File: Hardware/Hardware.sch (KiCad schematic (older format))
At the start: 1 part

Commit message: Some hardware dev
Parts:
- added C? (x2): C, symbol Device:C
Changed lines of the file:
@@
+	1    0    0    -1
+$EndComp
+$Comp
+L Device:C C?
+U 1 1 62087589
+P 3450 1550
+F 0 "C?" H 3565 1596 50  0000 L CNN
+F 1 "C" H 3565 1505 50  0000 L CNN
+F 2 "" H 3488 1400 50  0001 C CNN
+F 3 "~" H 3450 1550 50  0001 C CNN
+	1    3450 1550
+	1    0    0    -1
+$EndComp
+$Comp
+L Device:C C?
+U 1 1 620890B1
+P 2950 1550
+F 0 "C?" H 3065 1596 50  0000 L CNN
+F 1 "C" H 3065 1505 50  0000 L CNN
+F 2 "" H 2988 1400 50  0001 C CNN
+F 3 "~" H 2950 1550 50  0001 C CNN
+	1    2950 1550
 	1    0    0    -1
 $EndComp

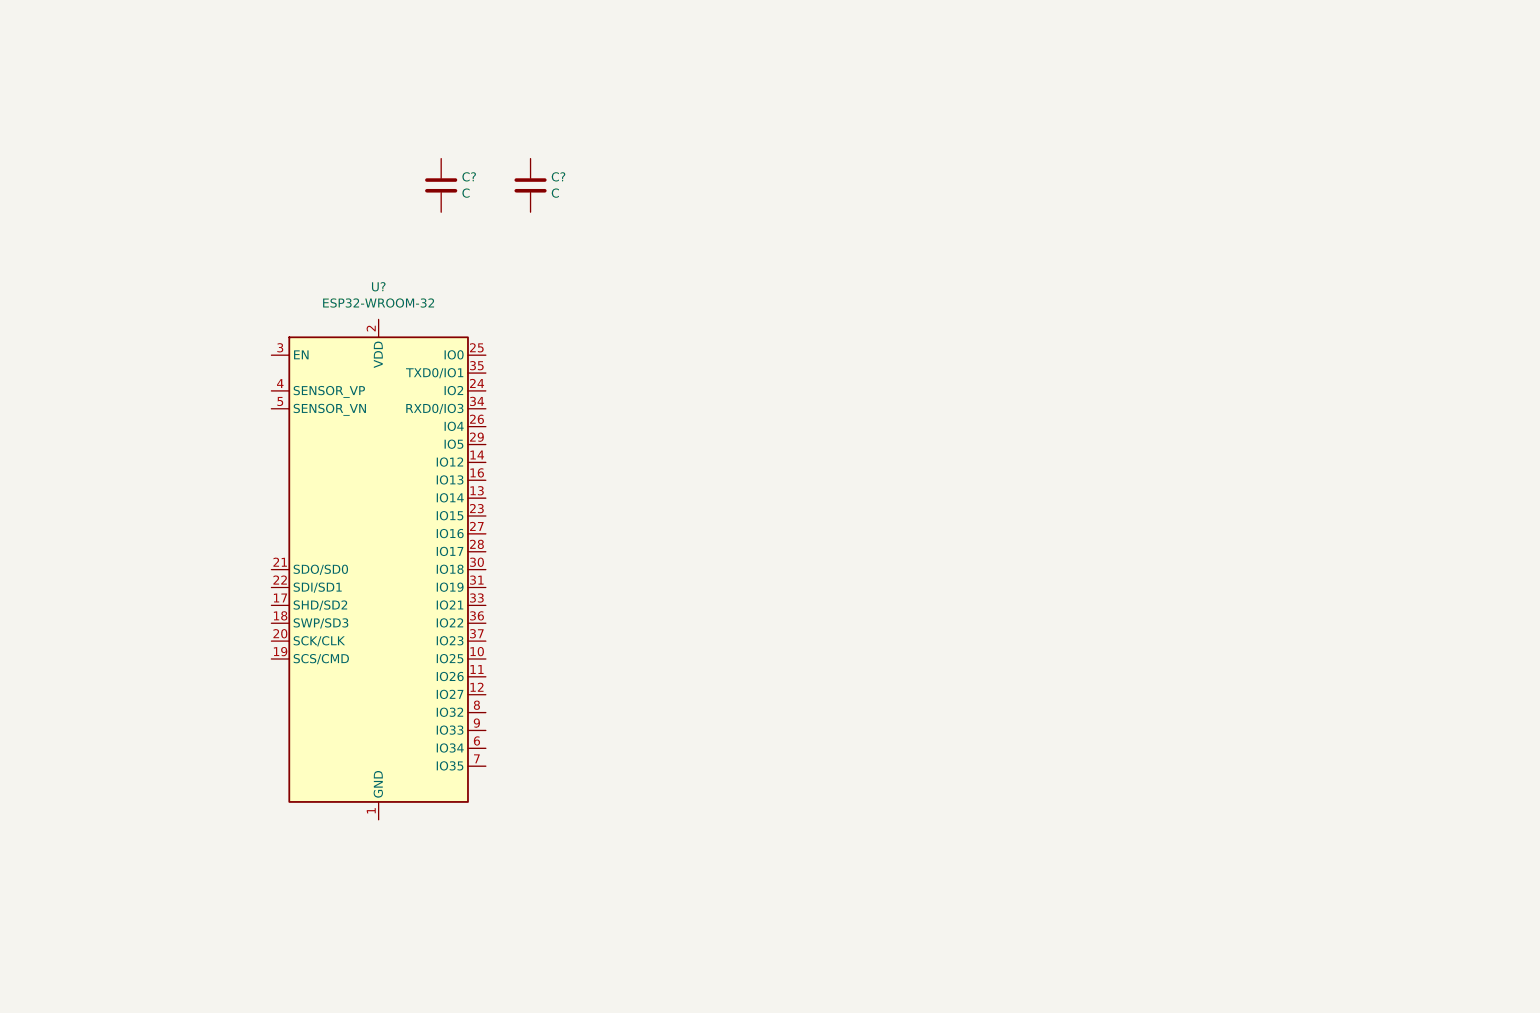
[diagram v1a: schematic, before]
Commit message: Basic hardware bringup for ESP32-WROOM
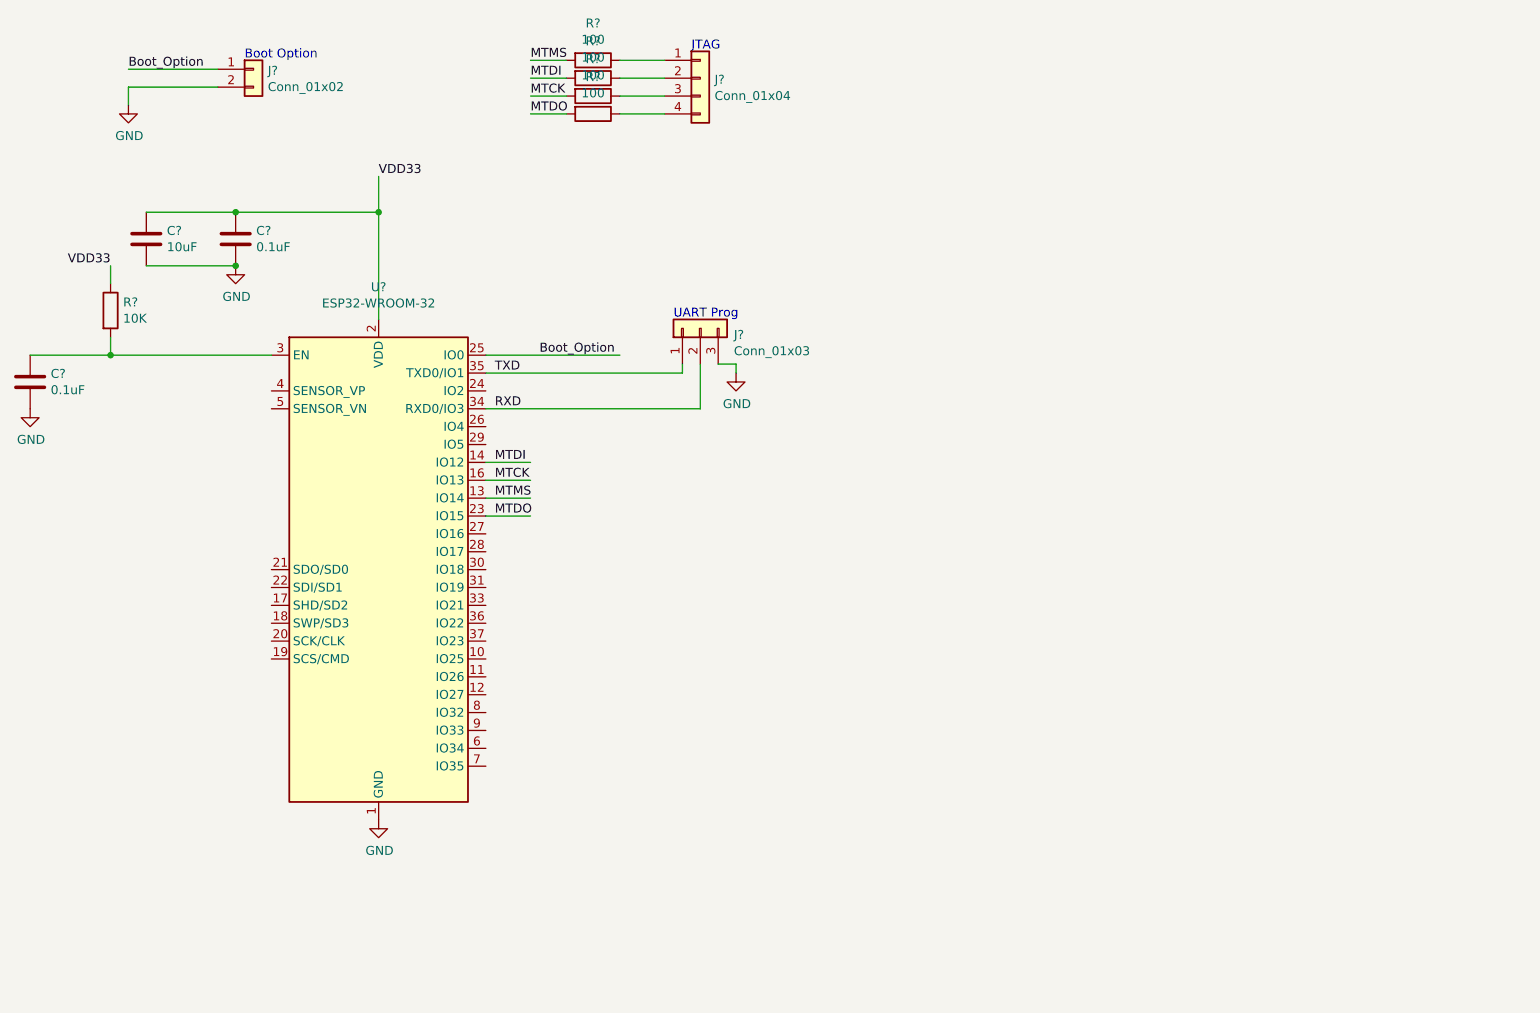
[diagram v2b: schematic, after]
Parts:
- removed C? (x2): C, symbol Device:C
- added C? (x2): 0.1uF, symbol Device:C
- added C?: 10uF, symbol Device:C
- added J?: Conn_01x02, symbol Connector_Generic:Conn_01x02
- added J?: Conn_01x03, symbol Connector_Generic:Conn_01x03
- added J?: Conn_01x04, symbol Connector_Generic:Conn_01x04
- added R?: 10K, symbol Device:R
- added R? (x4): 100, symbol Device:R
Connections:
- net labels added: Boot_Option, GND, MTCK, MTDI, MTDO, MTMS, RXD, TXD, VDD33
- wire segments 0 -> 31
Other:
- note added: "Boot Option\n"
- note added: "JTAG"
- note added: "UART Prog"

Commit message: Hardware dev
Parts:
- added J4: Conn_01x02, Connector_PinHeader_2.54mm:PinHeader_1x02_P2.54mm_Vertical, symbol Connector_Generic:Conn_01x02
- added J5: Conn_01x06, Connector_PinHeader_2.54mm:PinHeader_1x06_P2.54mm_Vertical, symbol Connector_Generic:Conn_01x06
- added J6: Conn_01x08, Connector_PinHeader_2.54mm:PinHeader_1x08_P2.54mm_Vertical, symbol Connector_Generic:Conn_01x08
- C1, C2, C3: renamed from C?; footprint (none) -> Connector_PinHeader_2.54mm:PinHeader_1x02_P2.54mm_Vertical
- J1: renamed from J?; footprint (none) -> Connector_PinHeader_2.54mm:PinHeader_1x02_P2.54mm_Vertical
- J2: renamed from J?; footprint (none) -> Connector_PinHeader_2.54mm:PinHeader_1x04_P2.54mm_Vertical
- J3: renamed from J?; footprint (none) -> Connector_PinHeader_2.54mm:PinHeader_1x03_P2.54mm_Vertical
- R1, R2, R3, R4, R5: renamed from R?; footprint (none) -> Connector_PinHeader_2.54mm:PinHeader_1x02_P2.54mm_Vertical
- gave numbers to parts that had none: 1
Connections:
- net labels added: GNDPWR, IO23, IO25, IO26, IO27, IO32, IO33, IO34, IO35, SCK, SCS, SDI, SDO, SHD, SWP
- wire segments 31 -> 56
- no-connect marks 0 -> 11
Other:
- note added: "Battery Input"
- note added: "IO Port"
- note added: "Serial Data Port"
- moved on the sheet: J1, J2, R2, R3, R4, R5

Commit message: Some footprints were fixed.
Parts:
- C1, C2, C3: footprint Connector_PinHeader_2.54mm:PinHeader_1x02_P2.54mm_Vertical -> Capacitor_THT:CP_Radial_D4.0mm_P2.00mm
- R1, R2, R3, R4, R5: footprint Connector_PinHeader_2.54mm:PinHeader_1x02_P2.54mm_Vertical -> Resistor_THT:R_Axial_DIN0204_L3.6mm_D1.6mm_P2.54mm_Vertical
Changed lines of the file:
@@
 F 0 "C3" H 1915 1896 50  0000 L CNN
 F 1 "0.1uF" H 1915 1805 50  0000 L CNN
-F 2 "Connector_PinHeader_2.54mm:PinHeader_1x02_P2.54mm_Vertical" H 1838 1700 50  0001 C CNN
+F 2 "Capacitor_THT:CP_Radial_D4.0mm_P2.00mm" H 1838 1700 50  0001 C CNN
 F 3 "~" H 1800 1850 50  0001 C CNN
 	1    1800 1850
@@
 F 0 "C2" H 1415 1896 50  0000 L CNN
 F 1 "10uF" H 1415 1805 50  0000 L CNN
-F 2 "Connector_PinHeader_2.54mm:PinHeader_1x02_P2.54mm_Vertical" H 1338 1700 50  0001 C CNN
+F 2 "Capacitor_THT:CP_Radial_D4.0mm_P2.00mm" H 1338 1700 50  0001 C CNN
 F 3 "~" H 1300 1850 50  0001 C CNN
 	1    1300 1850
 	1    0    0    -1
 $EndComp
-Wire Wire Line
-	1300 1700 1800 1700
 Wire Wire Line
 	1300 2000 1800 2000
@@
 	1    0    0    -1
 $EndComp
-Connection ~ 1800 2000
-Wire Wire Line
-	1800 1700 2600 1700
-Connection ~ 1800 1700
 Connection ~ 2600 1700
 Wire Wire Line
@@
 F 0 "R1" H 1170 2296 50  0000 L CNN
 F 1 "10K" H 1170 2205 50  0000 L CNN
-F 2 "Connector_PinHeader_2.54mm:PinHeader_1x02_P2.54mm_Vertical" V 1030 2250 50  0001 C CNN
+F 2 "Resistor_THT:R_Axial_DIN0204_L3.6mm_D1.6mm_P2.54mm_Vertical" V 1030 2250 50  0001 C CNN
 F 3 "~" H 1100 2250 50  0001 C CNN
 	1    1100 2250
@@
 F 0 "C1" H 765 2696 50  0000 L CNN
 F 1 "0.1uF" H 765 2605 50  0000 L CNN
-F 2 "Connector_PinHeader_2.54mm:PinHeader_1x02_P2.54mm_Vertical" H 688 2500 50  0001 C CNN
+F 2 "Capacitor_THT:CP_Radial_D4.0mm_P2.00mm" H 688 2500 50  0001 C CNN
 F 3 "~" H 650 2650 50  0001 C CNN
 	1    650  2650
@@
 F 0 "R2" V 5793 3850 50  0000 C CNN
 F 1 "100" V 5884 3850 50  0000 C CNN
-F 2 "Connector_PinHeader_2.54mm:PinHeader_1x02_P2.54mm_Vertical" V 5930 3850 50  0001 C CNN
+F 2 "Resistor_THT:R_Axial_DIN0204_L3.6mm_D1.6mm_P2.54mm_Vertical" V 5930 3850 50  0001 C CNN
 F 3 "~" H 6000 3850 50  0001 C CNN
 	1    6000 3850
@@
 F 0 "R3" V 5793 3950 50  0000 C CNN
 F 1 "100" V 5884 3950 50  0000 C CNN
-F 2 "Connector_PinHeader_2.54mm:PinHeader_1x02_P2.54mm_Vertical" V 5930 3950 50  0001 C CNN
+F 2 "Resistor_THT:R_Axial_DIN0204_L3.6mm_D1.6mm_P2.54mm_Vertical" V 5930 3950 50  0001 C CNN
 F 3 "~" H 6000 3950 50  0001 C CNN
 	1    6000 3950
@@
 F 0 "R4" V 5793 4050 50  0000 C CNN
 F 1 "100" V 5884 4050 50  0000 C CNN
-F 2 "Connector_PinHeader_2.54mm:PinHeader_1x02_P2.54mm_Vertical" V 5930 4050 50  0001 C CNN
+F 2 "Resistor_THT:R_Axial_DIN0204_L3.6mm_D1.6mm_P2.54mm_Vertical" V 5930 4050 50  0001 C CNN
 F 3 "~" H 6000 4050 50  0001 C CNN
 	1    6000 4050
@@
 F 0 "R5" V 5793 4150 50  0000 C CNN
 F 1 "100" V 5884 4150 50  0000 C CNN
-F 2 "Connector_PinHeader_2.54mm:PinHeader_1x02_P2.54mm_Vertical" V 5930 4150 50  0001 C CNN
+F 2 "Resistor_THT:R_Axial_DIN0204_L3.6mm_D1.6mm_P2.54mm_Vertical" V 5930 4150 50  0001 C CNN
 F 3 "~" H 6000 4150 50  0001 C CNN
 	1    6000 4150
@@
 Wire Wire Line
 	2600 5100 2600 5150
+Wire Wire Line
+	1300 1700 1800 1700
+Connection ~ 1800 1700
+Wire Wire Line
+	1800 1700 2600 1700
+Connection ~ 1800 2000
 $EndSCHEMATC
